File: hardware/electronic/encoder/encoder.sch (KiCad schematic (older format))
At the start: 10 parts, among them P1 CONN_01X04

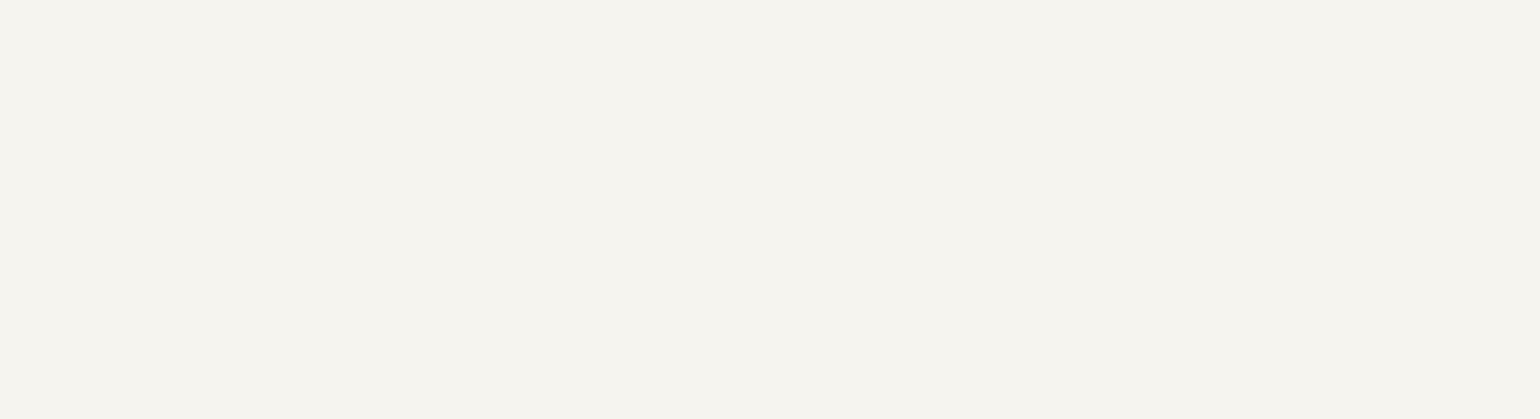
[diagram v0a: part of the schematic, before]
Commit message: HW: Add encoder rev-A production file and add KP entries
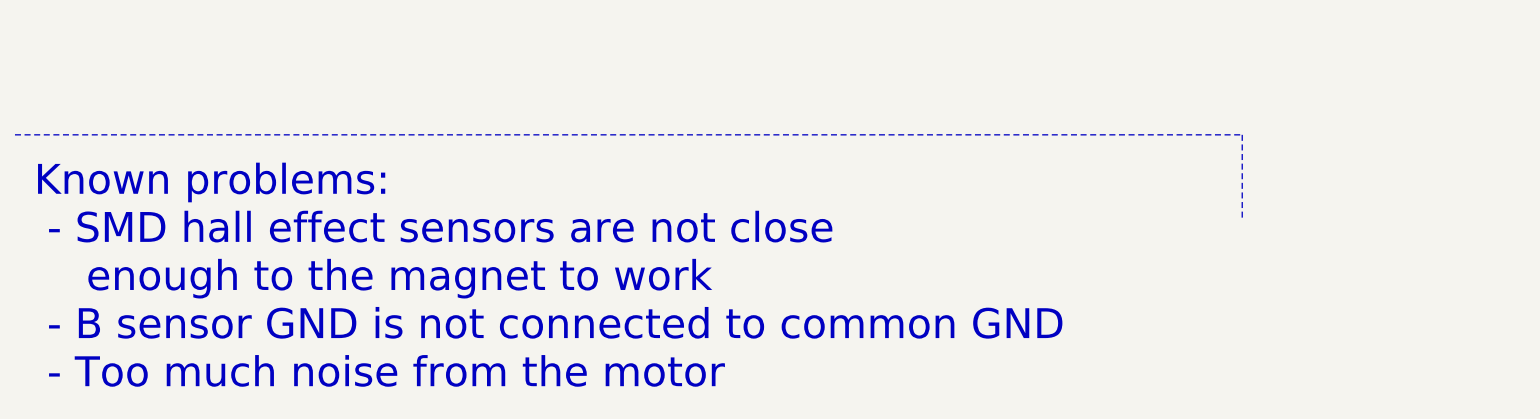
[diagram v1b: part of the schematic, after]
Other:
- note added: "Known problems:\n - SMD hall effect sensors are not close \n enough to the magnet to work\n - B sensor GND is not connected to common GND\n - Too much noise from the motor"
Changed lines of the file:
@@
 Wire Wire Line
 	7200 1950 7300 1950
+Text Notes 600  7450 0    157  ~ 0
+Known problems:\n - SMD hall effect sensors are not close \n    enough to the magnet to work\n - B sensor GND is not connected to common GND\n - Too much noise from the motor
+Wire Notes Line
+	500  6100 6950 6100
+Wire Notes Line
+	6950 6100 6950 6550
 $EndSCHEMATC

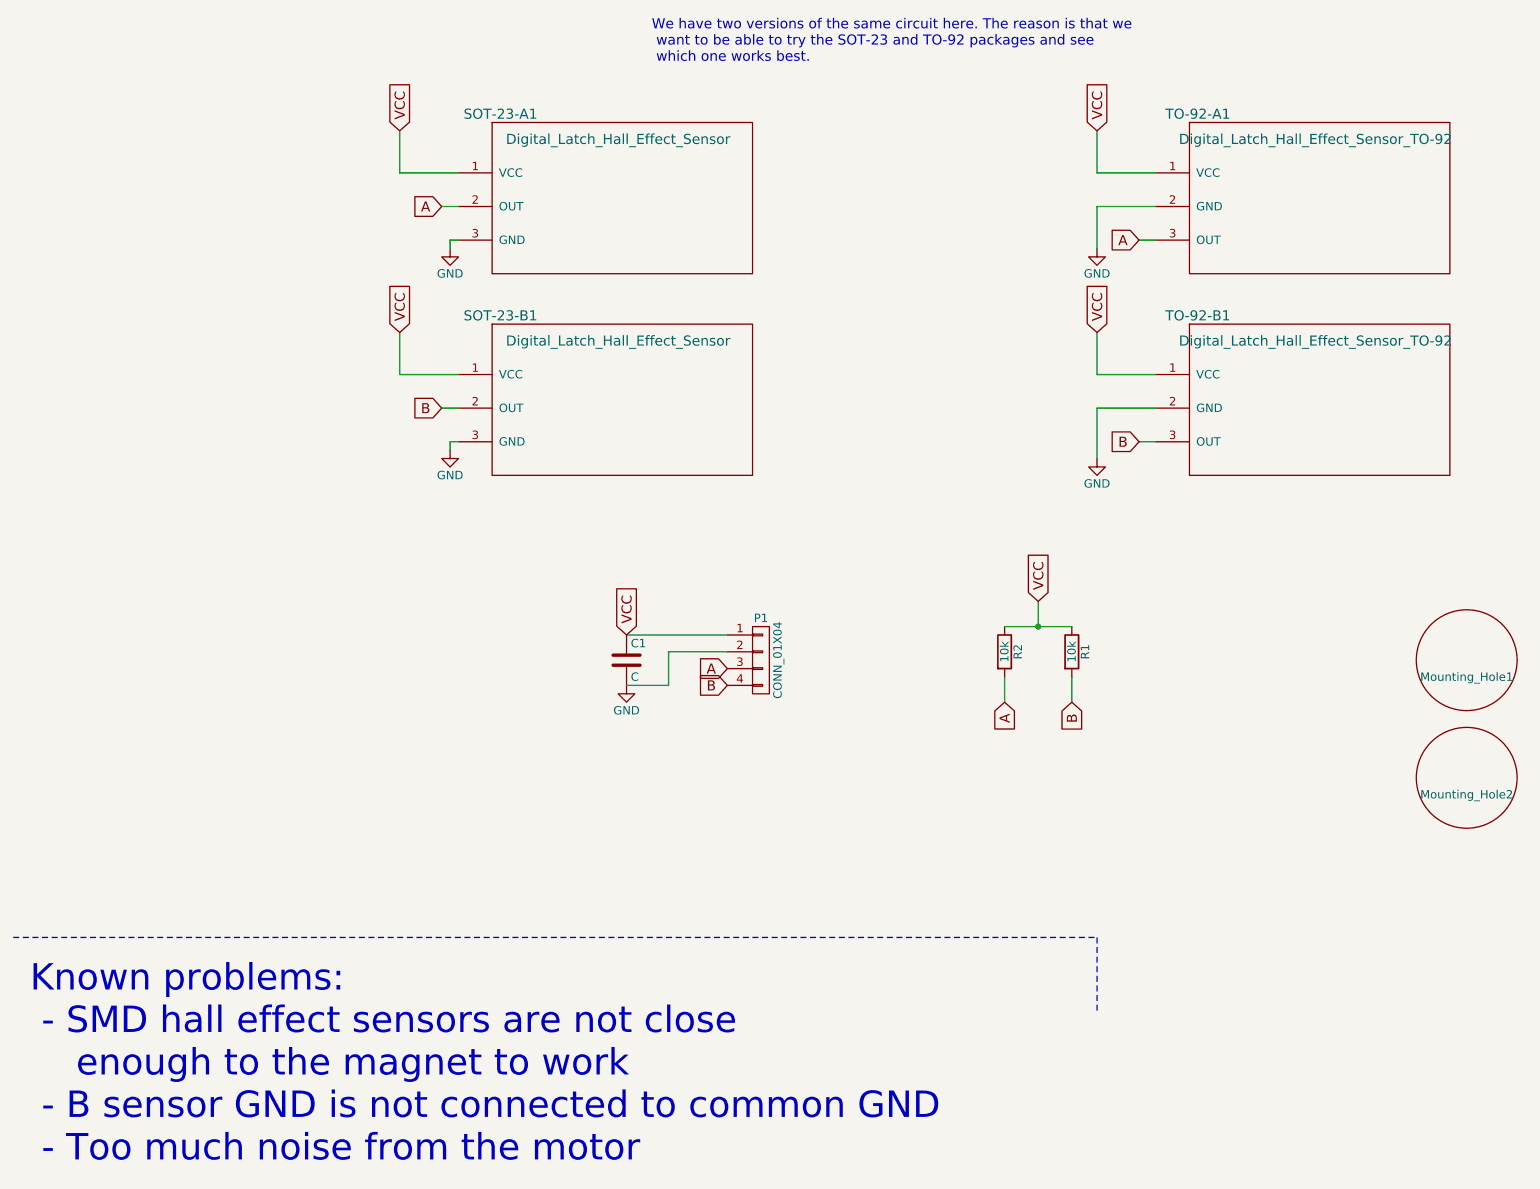
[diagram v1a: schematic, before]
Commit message: HW: Start encoder rev-B
 - Remove smd footprints
 - Use bigger pads for passives
 - Fix missing connection
 - Improve hall effect footprint and silkscreen
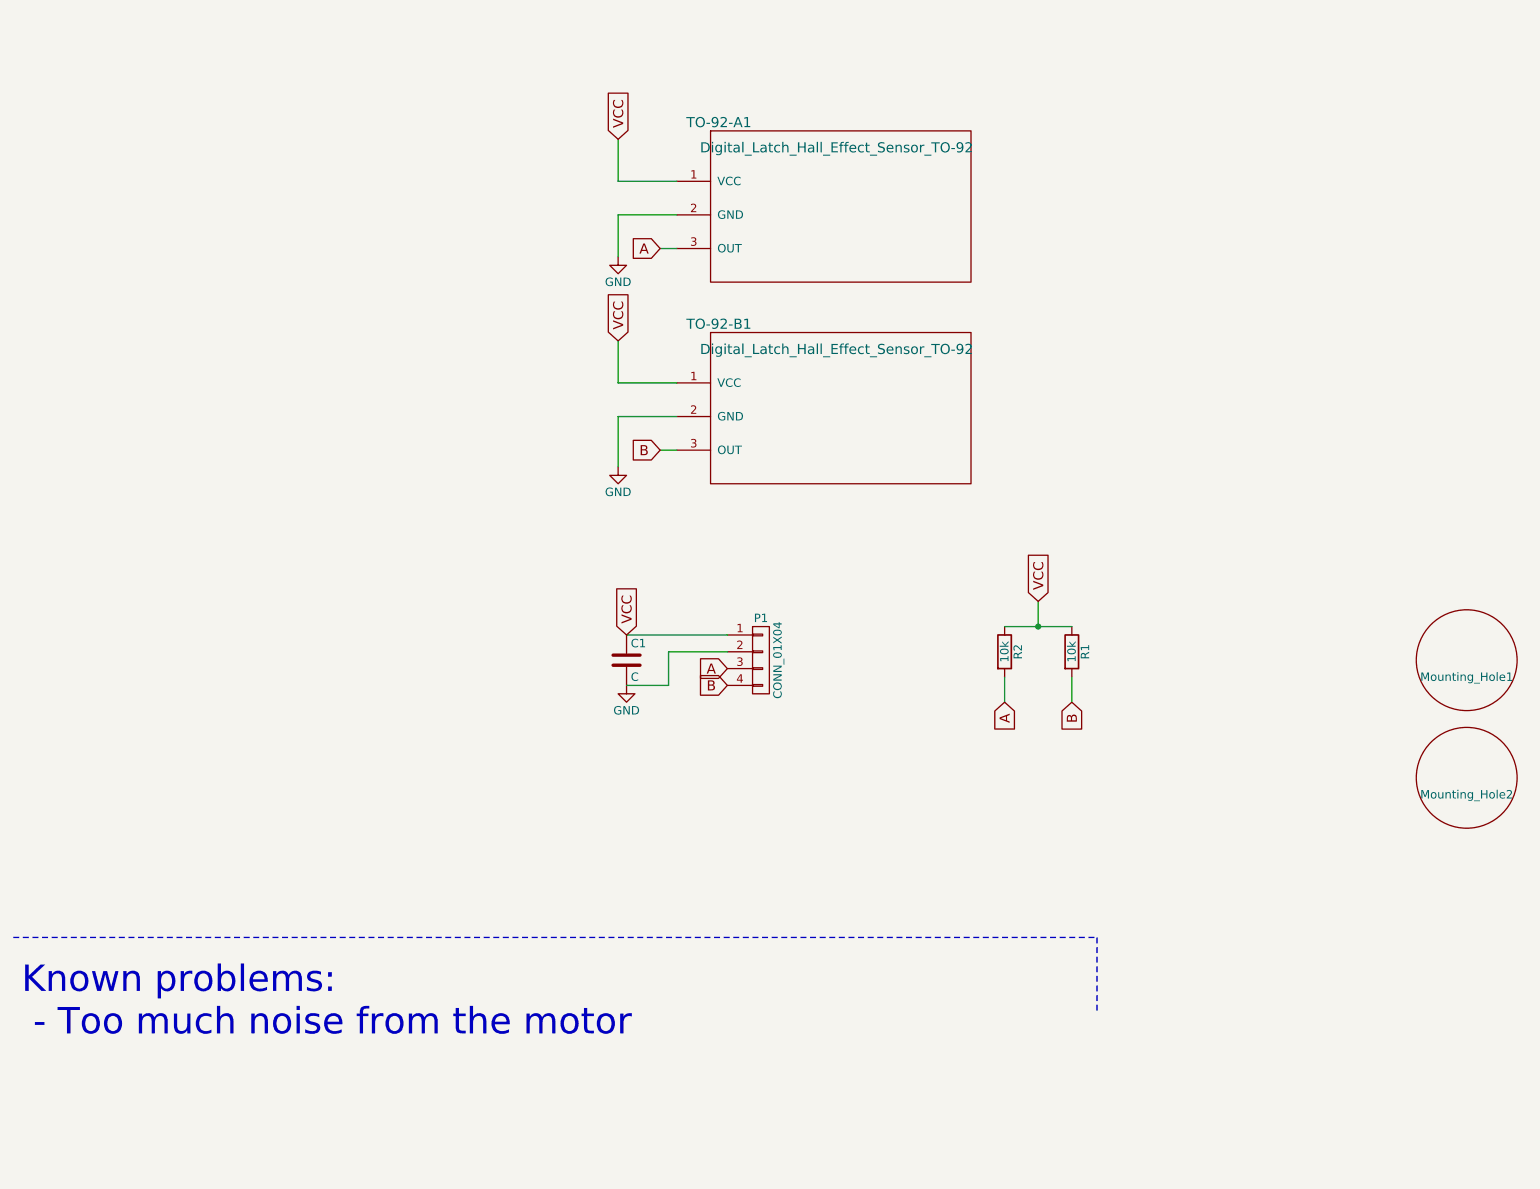
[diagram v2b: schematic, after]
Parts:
- removed SOT-23-A1, SOT-23-B1: Digital_Latch_Hall_Effect_Sensor, TO_SOT_Packages_SMD:SOT-23, symbol Digital_Latch_Hall_Effect_Sensor
- C1: footprint Capacitors_SMD:C_0805 -> Capacitors_SMD:C_0805_HandSoldering
- R1, R2: footprint Resistors_SMD:R_0805 -> Resistors_SMD:R_0805_HandSoldering
- TO-92-A1, TO-92-B1: footprint TO_SOT_Packages_THT:TO-92_Inline_Wide -> OPAVES:DRV5013_Hall_Sensor_TO-92_Inline
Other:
- note added: "Known problems:\n - Too much noise from the motor"
- note removed: "Known problems:\n - SMD hall effect sensors are not close \n enough to the magnet to work\n - B sensor GND is not connected to common GND\n - Too much noise from the motor"
- note removed: "We have two versions of the same circuit here. The reason is that we\n want to be able to try the SOT-23 and TO-92 packages and see\n which one works best."
- moved on the sheet: TO-92-A1, TO-92-B1
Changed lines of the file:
@@
 Title "O'PAVES - Encoders for TAMIYA High Speed Gearbox"
 Date ""
-Rev "A"
+Rev "B"
 Comp "AdaCore"
 Comment1 ""
@@
 $EndDescr
 $Comp
-L Digital_Latch_Hall_Effect_Sensor SOT-23-A1
-U 1 1 58889495
-P 3350 1250
-F 0 "SOT-23-A1" H 3400 1300 60  0000 C CNN
-F 1 "Digital_Latch_Hall_Effect_Sensor" H 4100 1150 60  0000 C CNN
-F 2 "TO_SOT_Packages_SMD:SOT-23" H 3350 1250 60  0001 C CNN
-F 3 "" H 3350 1250 60  0001 C CNN
-	1    3350 1250
-	1    0    0    -1
-$EndComp
-$Comp
-L Digital_Latch_Hall_Effect_Sensor SOT-23-B1
-U 1 1 5888965D
-P 3350 2450
-F 0 "SOT-23-B1" H 3400 2500 60  0000 C CNN
-F 1 "Digital_Latch_Hall_Effect_Sensor" H 4100 2350 60  0000 C CNN
-F 2 "TO_SOT_Packages_SMD:SOT-23" H 3350 2450 60  0001 C CNN
-F 3 "" H 3350 2450 60  0001 C CNN
-	1    3350 2450
-	1    0    0    -1
-$EndComp
-$Comp
 L R R1
 U 1 1 58889A60
@@
 F 0 "R1" V 6880 4400 50  0000 C CNN
 F 1 "10k" V 6800 4400 50  0000 C CNN
-F 2 "Resistors_SMD:R_0805" V 6730 4400 50  0001 C CNN
+F 2 "Resistors_SMD:R_0805_HandSoldering" V 6730 4400 50  0001 C CNN
 F 3 "" H 6800 4400 50  0000 C CNN
 	1    6800 4400
@@
 F 0 "C1" H 4175 4550 50  0000 L CNN
 F 1 "C" H 4175 4350 50  0000 L CNN
-F 2 "Capacitors_SMD:C_0805" H 4188 4300 50  0001 C CNN
+F 2 "Capacitors_SMD:C_0805_HandSoldering" H 4188 4300 50  0001 C CNN
 F 3 "" H 4150 4450 50  0000 C CNN
 	1    4150 4450
 	1    0    0    -1
 $EndComp
-Text GLabel 2800 1300 1    60   Input ~ 0
-VCC
 $Comp
 L R R2
@@
 F 0 "R2" V 6480 4400 50  0000 C CNN
 F 1 "10k" V 6400 4400 50  0000 C CNN
-F 2 "Resistors_SMD:R_0805" V 6330 4400 50  0001 C CNN
+F 2 "Resistors_SMD:R_0805_HandSoldering" V 6330 4400 50  0001 C CNN
 F 3 "" H 6400 4400 50  0000 C CNN
 	1    6400 4400
 	1    0    0    -1
 $EndComp
-Text GLabel 2800 2500 1    60   Input ~ 0
+Text GLabel 4100 1350 1    60   Input ~ 0
 VCC
-Text GLabel 6950 1300 1    60   Input ~ 0
-VCC
-Text GLabel 6950 2500 1    60   Input ~ 0
+Text GLabel 4100 2550 1    60   Input ~ 0
 VCC
 $Comp
 L GND #PWR01
-U 1 1 5888A135
-P 3100 2000
-F 0 "#PWR01" H 3100 1750 50  0001 C CNN
-F 1 "GND" H 3100 1850 50  0000 C CNN
-F 2 "" H 3100 2000 50  0000 C CNN
-F 3 "" H 3100 2000 50  0000 C CNN
-	1    3100 2000
+U 1 1 5888A1FD
+P 4100 3300
+F 0 "#PWR01" H 4100 3050 50  0001 C CNN
+F 1 "GND" H 4100 3150 50  0000 C CNN
+F 2 "" H 4100 3300 50  0000 C CNN
+F 3 "" H 4100 3300 50  0000 C CNN
+	1    4100 3300
 	1    0    0    -1
 $EndComp
 $Comp
 L GND #PWR02
-U 1 1 5888A1D7
-P 3100 3200
-F 0 "#PWR02" H 3100 2950 50  0001 C CNN
-F 1 "GND" H 3100 3050 50  0000 C CNN
-F 2 "" H 3100 3200 50  0000 C CNN
-F 3 "" H 3100 3200 50  0000 C CNN
-	1    3100 3200
-	1    0    0    -1
-$EndComp
-$Comp
-L GND #PWR03
-U 1 1 5888A1FD
-P 6950 3250
-F 0 "#PWR03" H 6950 3000 50  0001 C CNN
-F 1 "GND" H 6950 3100 50  0000 C CNN
-F 2 "" H 6950 3250 50  0000 C CNN
-F 3 "" H 6950 3250 50  0000 C CNN
-	1    6950 3250
-	1    0    0    -1
-$EndComp
-$Comp
-L GND #PWR04
 U 1 1 5888A27D
-P 6950 2000
-F 0 "#PWR04" H 6950 1750 50  0001 C CNN
-F 1 "GND" H 6950 1850 50  0000 C CNN
-F 2 "" H 6950 2000 50  0000 C CNN
-F 3 "" H 6950 2000 50  0000 C CNN
-	1    6950 2000
+P 4100 2050
+F 0 "#PWR02" H 4100 1800 50  0001 C CNN
+F 1 "GND" H 4100 1900 50  0000 C CNN
+F 2 "" H 4100 2050 50  0000 C CNN
+F 3 "" H 4100 2050 50  0000 C CNN
+	1    4100 2050
 	1    0    0    -1
 $EndComp
@@
 VCC
 $Comp
-L GND #PWR05
+L GND #PWR03
 U 1 1 5888A8C2
 P 4150 4600
-F 0 "#PWR05" H 4150 4350 50  0001 C CNN
+F 0 "#PWR03" H 4150 4350 50  0001 C CNN
 F 1 "GND" H 4150 4450 50  0000 C CNN
 F 2 "" H 4150 4600 50  0000 C CNN
@@
 $EndComp
 Wire Wire Line
-	2800 1550 3150 1550
+	4100 1600 4450 1600
 Wire Wire Line
-	2800 1300 2800 1550
+	4100 1350 4100 1600
 Wire Wire Line
-	2800 2500 2800 2750
+	4100 2800 4450 2800
 Wire Wire Line
-	6950 1550 7300 1550
-Wire Wire Line
-	6950 1300 6950 1550
-Wire Wire Line
-	6950 2750 7300 2750
-Wire Wire Line
-	6950 2500 6950 2750
-Wire Wire Line
-	3150 1950 3100 1950
-Wire Wire Line
-	3100 1950 3100 2000
-Wire Wire Line
-	3150 3150 3100 3150
-Wire Wire Line
-	3100 3150 3100 3200
+	4100 2550 4100 2800
 Wire Wire Line
 	4750 4300 4150 4300
@@
 Text GLabel 4750 4600 0    60   Input ~ 0
 B
-Text GLabel 3050 1750 0    60   Input ~ 0
+Text GLabel 4350 2000 0    60   Input ~ 0
 A
-Text GLabel 3050 2950 0    60   Input ~ 0
+Text GLabel 4350 3200 0    60   Input ~ 0
 B
-Text GLabel 7200 1950 0    60   Input ~ 0
-A
-Text GLabel 7200 3150 0    60   Input ~ 0
-B
-Text Notes 4300 900  0    60   ~ 0
-We have two versions of the same circuit here. The reason is that we\n want to be able to try the SOT-23 and TO-92 packages and see\n which one works best.
-Wire Wire Line
-	2800 2750 3150 2750
-Wire Wire Line
-	3150 2950 3050 2950
 Wire Wire Line
 	6800 4250 6400 4250
@@
 Text GLabel 6600 4100 1    60   Input ~ 0
 VCC
-Wire Wire Line
-	3050 1750 3150 1750
 Text GLabel 6400 4700 3    60   Input ~ 0
 A
@@
 L Digital_Latch_Hall_Effect_Sensor_TO-92 TO-92-A1
 U 1 1 5888CFCF
-P 7500 1250
-F 0 "TO-92-A1" H 7550 1300 60  0000 C CNN
-F 1 "Digital_Latch_Hall_Effect_Sensor_TO-92" H 8250 1150 60  0000 C CNN
-F 2 "TO_SOT_Packages_THT:TO-92_Inline_Wide" H 7500 1250 60  0001 C CNN
-F 3 "" H 7500 1250 60  0001 C CNN
-	1    7500 1250
+P 4650 1300
+F 0 "TO-92-A1" H 4700 1350 60  0000 C CNN
+F 1 "Digital_Latch_Hall_Effect_Sensor_TO-92" H 5400 1200 60  0000 C CNN
+F 2 "OPAVES:DRV5013_Hall_Sensor_TO-92_Inline" H 4650 1300 60  0001 C CNN
+F 3 "" H 4650 1300 60  0001 C CNN
+	1    4650 1300
 	1    0    0    -1
 $EndComp
@@
 L Digital_Latch_Hall_Effect_Sensor_TO-92 TO-92-B1
 U 1 1 5888D106
-P 7500 2450
-F 0 "TO-92-B1" H 7550 2500 60  0000 C CNN
-F 1 "Digital_Latch_Hall_Effect_Sensor_TO-92" H 8250 2350 60  0000 C CNN
-F 2 "TO_SOT_Packages_THT:TO-92_Inline_Wide" H 7500 2450 60  0001 C CNN
-F 3 "" H 7500 2450 60  0001 C CNN
-	1    7500 2450
+P 4650 2500
+F 0 "TO-92-B1" H 4700 2550 60  0000 C CNN
+F 1 "Digital_Latch_Hall_Effect_Sensor_TO-92" H 5400 2400 60  0000 C CNN
+F 2 "OPAVES:DRV5013_Hall_Sensor_TO-92_Inline" H 4650 2500 60  0001 C CNN
+F 3 "" H 4650 2500 60  0001 C CNN
+	1    4650 2500
 	1    0    0    -1
 $EndComp
 Wire Wire Line
-	7200 3150 7300 3150
+	4350 3200 4450 3200
 Wire Wire Line
-	7300 2950 6950 2950
+	4450 3000 4100 3000
 Wire Wire Line
-	6950 2950 6950 3250
+	4100 3000 4100 3300
 Wire Wire Line
-	6950 2000 6950 1750
+	4100 2050 4100 1800
 Wire Wire Line
-	6950 1750 7300 1750
+	4100 1800 4450 1800
 Wire Wire Line
-	7200 1950 7300 1950
-Text Notes 600  7450 0    157  ~ 0
-Known problems:\n - SMD hall effect sensors are not close \n    enough to the magnet to work\n - B sensor GND is not connected to common GND\n - Too much noise from the motor
+	4350 2000 4450 2000
+Text Notes 550  6700 0    157  ~ 0
+Known problems:\n - Too much noise from the motor
 Wire Notes Line
 	500  6100 6950 6100

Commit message: HW: Encoder rev-B
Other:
- note added: "Known problems:\n"
- note removed: "Known problems:\n - Too much noise from the motor"
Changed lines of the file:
@@
 Wire Wire Line
 	4350 2000 4450 2000
-Text Notes 550  6700 0    157  ~ 0
-Known problems:\n - Too much noise from the motor
+Text Notes 550  6350 0    157  ~ 0
+Known problems:\n
 Wire Notes Line
 	500  6100 6950 6100
